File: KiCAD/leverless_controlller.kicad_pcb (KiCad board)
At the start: 2 copper layers, 251.4 x 138.3 mm, 31 parts, among them SW2 SW_Push, U1 RP2040, U2 NCP1117-3.3_SOT223, U3 W25Q16JVSS, Y1 ABM8-272-T3

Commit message: Start PCB Layout
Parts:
- added J1: USB_C_Receptacle_USB2.0_14P, Fightstick_Library:USB_C_Receptacle_HCTL_Fightstick_16P_TopMnt_Horizontal, F.Cu at (76.4, 30.7)
- added SW10_SHARE1: SW_Push, Fightstick_Library:Kailh_MX_Style_Keyswitch, F.Cu at (257.2, 46.9)
- added SW11_START1: SW_Push, Fightstick_Library:Kailh_MX_Style_Keyswitch, F.Cu at (257.2, 63.1)
- added SW12_THROW1: SW_Push, Fightstick_Library:Kailh_MX_Style_Keyswitch, F.Cu at (149.9, 60.3)
- added SW13_R3: SW_Push, Fightstick_Library:Kailh_MX_Style_Keyswitch, F.Cu at (257.2, 95.4)
- added SW14_PS1: SW_Push, Fightstick_Library:Kailh_MX_Style_Keyswitch, F.Cu at (257.2, 111.5)
- added SW15_TOUCHPAD1: SW_Push, Fightstick_Library:Kailh_MX_Style_Keyswitch, F.Cu at (257.2, 127.7)
- added SW16_UP1: SW_Push, Fightstick_Library:Kailh_MX_Style_Keyswitch, F.Cu at (150.4, 136.0)
- added SW17_UP2: SW_Push, Fightstick_Library:Kailh_MX_Style_Keyswitch, F.Cu at (117.1, 54.4)
- added SW18_DOWN1: SW_Push, Fightstick_Library:Kailh_MX_Style_Keyswitch, F.Cu at (109.8, 72.0)
- added SW19_LEFT1: SW_Push, Fightstick_Library:Kailh_MX_Style_Keyswitch, F.Cu at (92.2, 64.7)
- added SW20_RIGHT1: SW_Push, Fightstick_Library:Kailh_MX_Style_Keyswitch, F.Cu at (125.9, 83.0)
- added SW3_MK1: SW_Push, Fightstick_Library:Kailh_MX_Style_Keyswitch, F.Cu at (199.9, 90.0)
- added SW4_LP1: SW_Push, Fightstick_Library:Kailh_MX_Style_Keyswitch, F.Cu at (174.9, 75.0)
- added SW5_MP1: SW_Push, Fightstick_Library:Kailh_MX_Style_Keyswitch, F.Cu at (199.9, 61.0)
- added SW6_DI1: SW_Push, Fightstick_Library:Kailh_MX_Style_Keyswitch, F.Cu at (175.1, 46.0)
- added SW7_HP1: SW_Push, Fightstick_Library:Kailh_MX_Style_Keyswitch, F.Cu at (228.9, 61.0)
- added SW8_DP1: SW_Push, Fightstick_Library:Kailh_MX_Style_Keyswitch, F.Cu at (60.0, 72.0)
- added SW9_HK1: SW_Push, Fightstick_Library:Kailh_MX_Style_Keyswitch, F.Cu at (228.9, 90.0)
- S1: footprint keyswitches.pretty-2.1:Stabilizer_MX_2u -> Fightstick_Library:Kailh_MX_Style_Keyswitch
- SW2_LK1: renamed from SW2; footprint keyswitches.pretty-2.1:Kailh_socket_MX -> Fightstick_Library:Kailh_MX_Style_Keyswitch
- moved C2 100.1 mm to (59.9, 40.6), turned to 180 degrees
- moved C1 94.0 mm to (68.9, 35.7), turned to 180 degrees
- moved R1 92.3 mm to (69.5, 33.7), turned to 180 degrees
- moved U2 90.5 mm to (65.9, 40.7), turned to 180 degrees
- moved C5 89.7 mm to (72.9, 45.5), turned to 180 degrees
- moved R2 87.8 mm to (73.9, 37.2), turned to -90 degrees
- moved R6 87.6 mm to (70.6, 50.4), turned to -90 degrees
- moved R5 87.1 mm to (68.3, 53.1)
- moved R3 86.1 mm to (78.4, 36.3)
- moved SW2_LK1 75.7 mm to (174.9, 104.0)
- moved C4 74.8 mm to (95.9, 39.4), turned to 180 degrees
- moved R4 73.4 mm to (91.4, 42.9), turned to 180 degrees
- moved C17 68.6 mm to (83.6, 36.3), turned to 90 degrees
- moved C3 68.5 mm to (99.0, 43.2), turned to -90 degrees
- moved C16 67.2 mm to (82.5, 36.3), turned to 90 degrees
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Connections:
- SW2_LK1 pad 1: A1 -> B1
- U1 pad 34: unconnected-(U1-GPIO22-Pad34) -> UP2
- U1 pad 4: UP -> UP1
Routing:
- net +3.3V: track 0.00 -> 66.5 mm
- net /Main/QSPI_SS: track 0.00 -> 28.9 mm
- net +1V1: track 0.00 -> 18.2 mm
- net /Main/QSPI_SD1: track 0.00 -> 15.2 mm
- net /Main/XIN: track 0.00 -> 12.4 mm
- net /Main/QSPI_SD2: track 0.00 -> 11.9 mm
- net VBUS: track 0.00 -> 10.8 mm
- net /Main/D+: track 0.00 -> 10.6 mm
- net /Main/D-: track 0.00 -> 8.32 mm
- net /Main/QSPI_SD3: track 0.00 -> 6.70 mm
- net /Main/QSPI_SCLK: track 0.00 -> 6.15 mm
- net Net-(C4-Pad2): track 0.00 -> 6.10 mm
- net /Main/QSPI_SD0: track 0.00 -> 4.63 mm
- net /Main/XOUT: track 0.00 -> 3.02 mm
- net Net-(U1-USB_DP): track 0.00 -> 2.55 mm
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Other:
- board outline removed

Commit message: PCB First Draft
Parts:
- removed C17: 100n, Capacitor_SMD:C_0402_1005Metric
- removed SW13_R3: SW_Push, Fightstick_Library:Kailh_MX_Style_Keyswitch
- added ?: , , F.Cu at (83.8, 41.9)
- added ?: , , F.Cu at (85.9, 41.9)
- added ?: , , F.Cu at (85.9, 40.9)
- added ?: , , F.Cu at (85.9, 42.9)
- added ?: , , F.Cu at (84.8, 42.9)
- added ?: , , F.Cu at (84.8, 40.9)
- added ?: , , F.Cu at (84.8, 41.9)
- added ?: , , F.Cu at (83.8, 42.9)
- added ?: , , F.Cu at (83.8, 40.9)
- added J2: Conn_01x03_Socket, Fightstick_Library:Debug_Points, F.Cu at (97.8, 36.5)
- added SW1: SW_DIP_x01, Fightstick_Library:SW_SMD_BUTTON_YTS_A007, F.Cu at (55.2, 37.2)
- added SW2_MODE1: SW_SPST, Button_Switch_THT:SW_SPST_Omron_B3F-40xx, F.Cu at (58.0, 51.0)
- S1: footprint Fightstick_Library:Kailh_MX_Style_Keyswitch -> PCM_Mounting_Keyboard_Stabilizer:Stabilizer_Cherry_MX_2.00u
- SW10_SHARE1, SW11_START1, SW14_PS1, SW15_TOUCHPAD1: footprint Fightstick_Library:Kailh_MX_Style_Keyswitch -> Button_Switch_THT:SW_SPST_Omron_B3F-40xx
- moved SW15_TOUCHPAD1 82.7 mm to (242.5, 46.2), turned to 90 degrees
- moved SW14_PS1 71.7 mm to (227.5, 46.2), turned to 90 degrees
- moved SW11_START1 62.0 mm to (197.5, 46.2), turned to 90 degrees
- moved SW10_SHARE1 44.7 mm to (212.5, 46.2), turned to 90 degrees
- moved S1 37.2 mm to (150.4, 136.0)
- moved C5 6.90 mm to (72.1, 52.3), turned to 0 degrees
- moved R5 6.75 mm to (63.9, 48.0)
- moved C2 5.43 mm to (62.9, 36.1), turned to 90 degrees
- moved R6 3.08 mm to (67.7, 49.4)
- moved U3 2.62 mm to (74.9, 48.5), turned to 180 degrees
- moved R4 1.14 mm to (92.6, 42.9)
- moved C16 1.00 mm to (83.5, 36.0)
- moved C3 0.90 mm to (99.0, 42.3)
- moved Y1 0.90 mm to (96.3, 41.6)
- moved C4 0.90 mm to (95.9, 38.5)
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- renumbered SW16_UP1 to SW16_SPACE1, SW17_UP2 to SW17_W1
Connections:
- net UP1 renamed SPACE
- SW17_W1 pad 1: UP2 -> W
- U1 pad 11: R2 -> B2
- U1 pad 12: L2 -> R2
- U1 pad 14: B4 -> L3
- U1 pad 15: R1 -> B4
- U1 pad 16: L1 -> R1
- U1 pad 17: TURBO -> A2
- U1 pad 18: T LED -> unconnected-(U1-GPIO15-Pad18)
- U1 pad 2: SDA -> MODE
- U1 pad 26: /Main/RUN -> +3.3V
- U1 pad 27: S1 -> A1
- U1 pad 28: S2 -> L1
- U1 pad 29: L3 -> S1
- U1 pad 3: SLC -> L2
- U1 pad 30: R3 -> S2
- U1 pad 31: A1 -> unconnected-(U1-GPIO20-Pad31)
- U1 pad 32: A2 -> unconnected-(U1-GPIO21-Pad32)
- U1 pad 34: UP2 -> unconnected-(U1-GPIO22-Pad34)
- U1 pad 5: DOWN -> LEFT
- U1 pad 6: RIGHT -> DOWN
- U1 pad 7: LEFT -> RIGHT
- U1 pad 8: B1 -> W
- U1 pad 9: B2 -> B1
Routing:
- net GND: track 0.00 -> 654.5 mm, vias 0 -> 11
- net A2: track 0.00 -> 171.3 mm
- net R2: track 0.00 -> 166.8 mm, vias 0 -> 1
- net A1: track 0.00 -> 160.8 mm
- net R1: track 0.00 -> 153.1 mm, vias 0 -> 1
- net S1: track 0.00 -> 141.1 mm
- net B2: track 0.00 -> 138.7 mm, vias 0 -> 1
- net B4: track 0.00 -> 134.2 mm, vias 0 -> 1
- net S2: track 0.00 -> 127.0 mm
- net B1: track 0.00 -> 124.7 mm, vias 0 -> 1
- net SPACE: track 0.00 -> 124.7 mm, vias 0 -> 1
- net B3: track 0.00 -> 106.0 mm, vias 0 -> 1
- net L1: track 0.00 -> 99.0 mm, vias 0 -> 1
- net +3.3V: track 66.5 -> 144.8 mm, vias 0 -> 5
- net L3: track 0.00 -> 74.4 mm, vias 0 -> 1
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- added copper zone on B.Cu, net GND
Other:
- board outline added: 213 x 123 mm

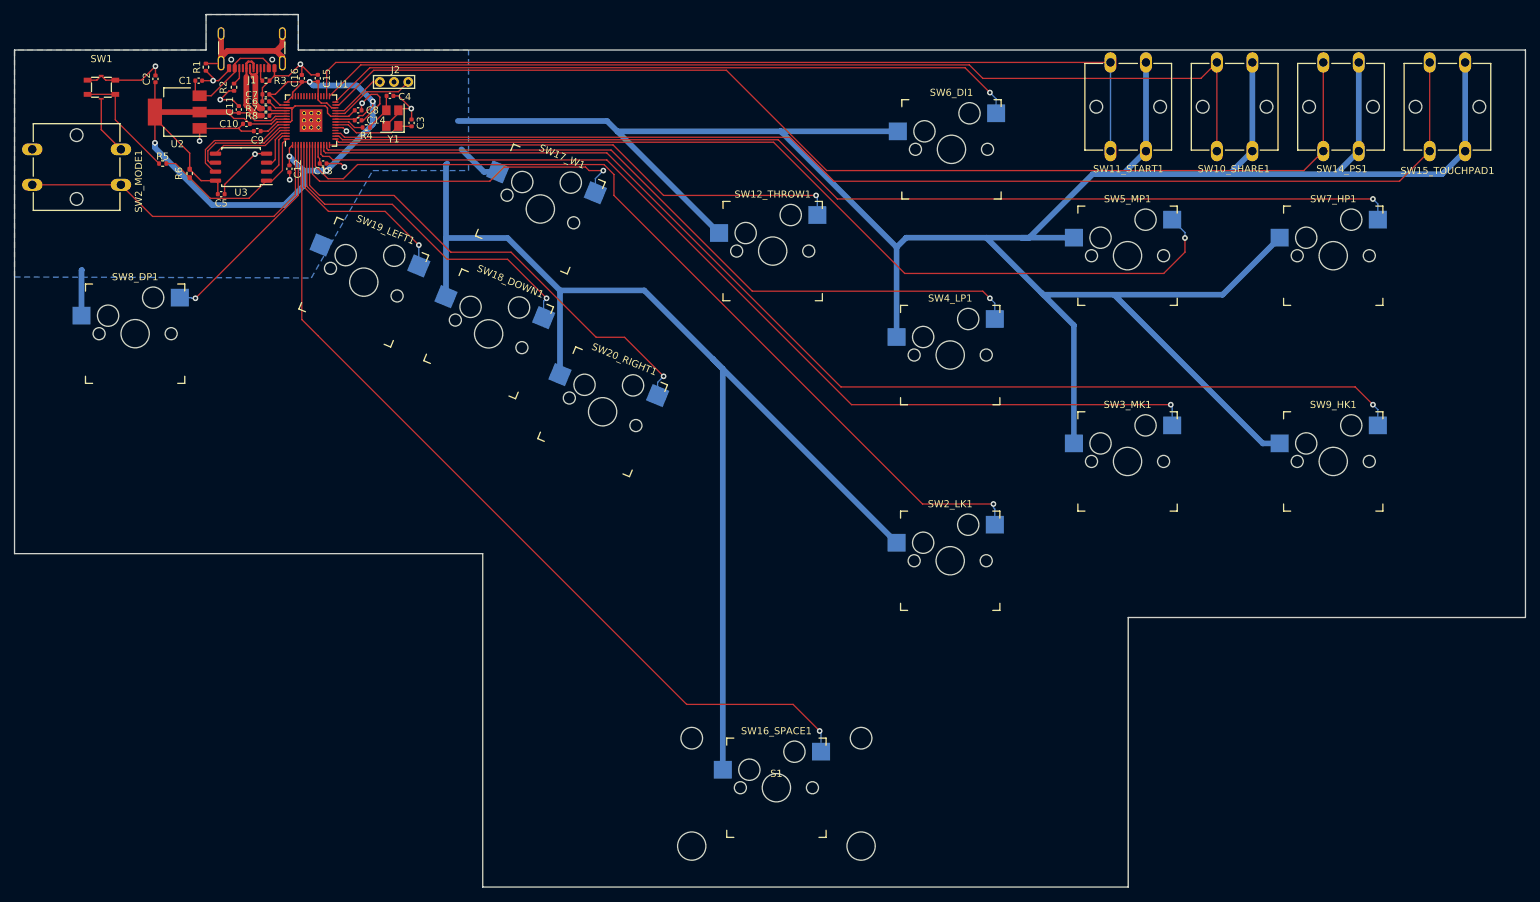
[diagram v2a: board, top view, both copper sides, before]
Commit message: Make PCB and case fit together
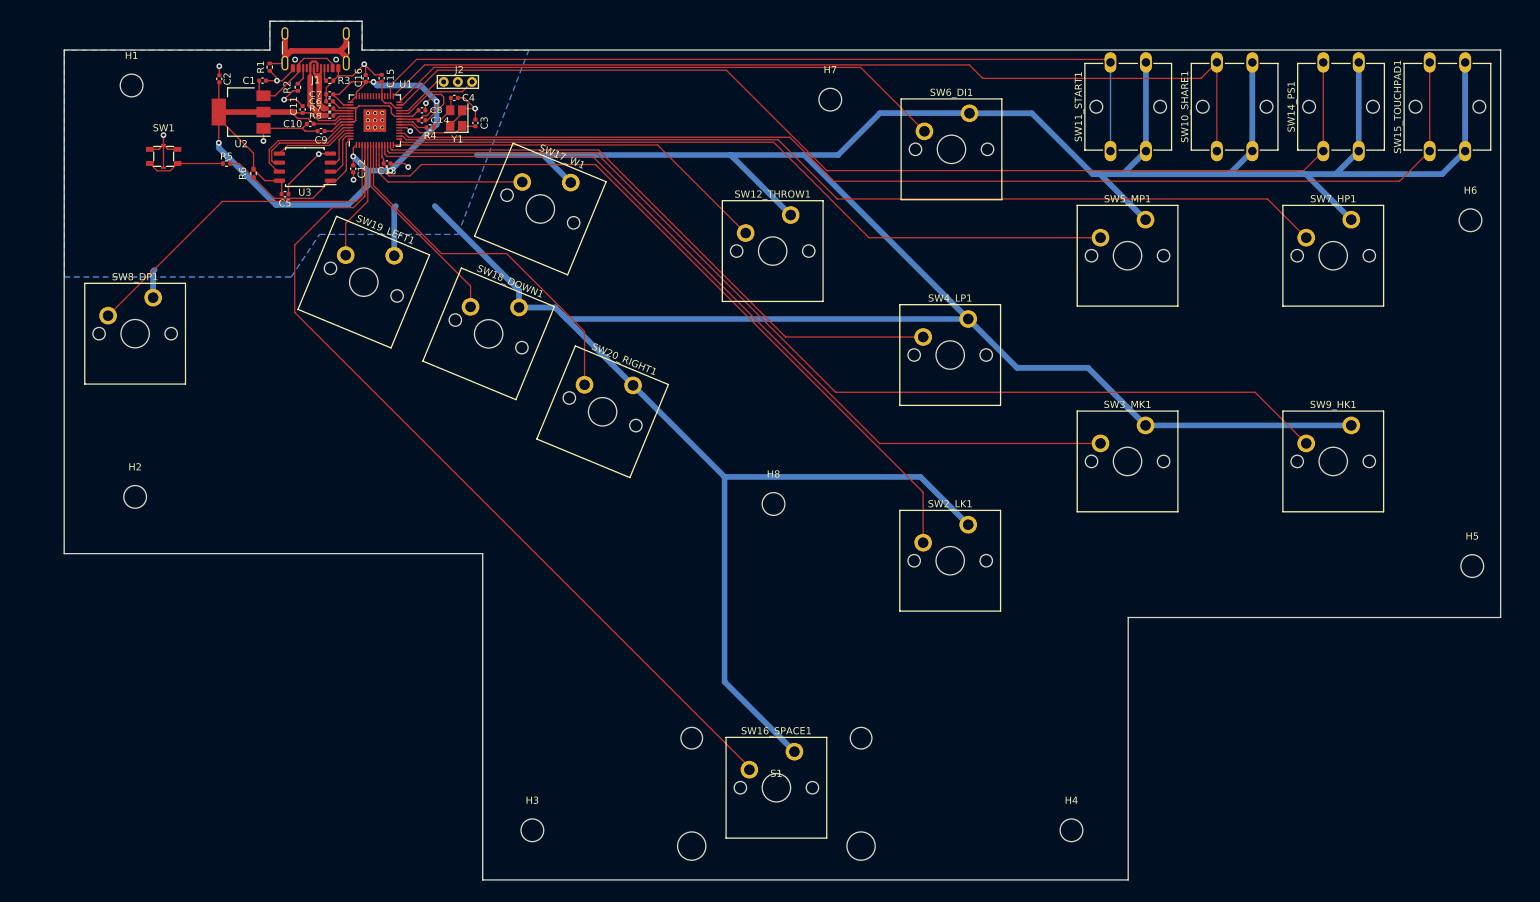
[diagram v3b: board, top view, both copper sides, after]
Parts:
- removed SW2_MODE1: SW_SPST, Button_Switch_THT:SW_SPST_Omron_B3F-40xx
- added H1: MountingHole, MountingHole:MountingHole_3.2mm_M3, F.Cu at (59.5, 37.0)
- added H2: MountingHole, MountingHole:MountingHole_3.2mm_M3, F.Cu at (60.0, 95.0)
- added H3: MountingHole, MountingHole:MountingHole_3.2mm_M3, F.Cu at (116.0, 142.0)
- added H4: MountingHole, MountingHole:MountingHole_3.2mm_M3, F.Cu at (192.0, 142.0)
- added H5: MountingHole, MountingHole:MountingHole_3.2mm_M3, F.Cu at (248.5, 104.8)
- added H6: MountingHole, MountingHole:MountingHole_3.2mm_M3, F.Cu at (248.2, 56.0)
- added H7: MountingHole, MountingHole:MountingHole_3.2mm_M3, F.Cu at (158.0, 39.0)
- added H8: MountingHole, MountingHole:MountingHole_3.2mm_M3, F.Cu at (150.0, 96.0)
- SW12_THROW1, SW16_SPACE1, SW2_LK1, SW3_MK1, SW4_LP1, SW5_MP1, SW6_DI1, SW7_HP1, SW8_DP1, SW9_HK1: footprint Fightstick_Library:Kailh_MX_Style_Keyswitch -> PCM_Switch_Keyboard_Cherry_MX:SW_Cherry_MX_PCB
- SW17_W1, SW18_DOWN1, SW19_LEFT1, SW20_RIGHT1: footprint Fightstick_Library:Kailh_MX_Style_Keyswitch -> PCM_Switch_Keyboard_Cherry_MX:SW_Cherry_MX_PCB_1.00u
- moved SW1 13.1 mm to (64.0, 47.0)
- moved C4 9.08 mm to (105.0, 38.8)
- moved ? 9.00 mm to (92.8, 41.9)
- moved ? 9.00 mm to (94.9, 41.9)
- moved ? 9.00 mm to (94.9, 40.9)
- moved ? 9.00 mm to (94.9, 42.9)
- moved ? 9.00 mm to (93.8, 42.9)
- moved ? 9.00 mm to (93.8, 40.9)
- moved ? 9.00 mm to (93.8, 41.9)
- moved ? 9.00 mm to (92.8, 42.9)
- moved ? 9.00 mm to (92.8, 40.9)
- moved C1 9.00 mm to (78.0, 36.3)
- moved C10 9.00 mm to (84.7, 42.4)
- moved C11 9.00 mm to (83.6, 40.4)
- moved C12 9.00 mm to (90.8, 48.8)
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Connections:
- U1 pad 2: MODE -> unconnected-(U1-GPIO0-Pad2)
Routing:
- net MODE: track 47.2 -> 0.00 mm
- net B4: track 134.2 -> 104.6 mm, vias 1 -> 0
- net GND: track 654.5 -> 628.0 mm, vias 11 -> 12
- net W: track 50.2 -> 24.8 mm, vias 1 -> 0
- net DOWN: track 49.1 -> 28.7 mm, vias 1 -> 0
- net L2: track 29.9 -> 49.9 mm, vias 1 -> 0
- net B2: track 138.7 -> 119.1 mm, vias 1 -> 0
- net L3: track 74.4 -> 54.8 mm, vias 1 -> 0
- net R2: track 166.8 -> 147.4 mm, vias 1 -> 0
- net R1: track 153.1 -> 133.8 mm, vias 1 -> 0
- net B3: track 106.0 -> 86.6 mm, vias 1 -> 0
- net L1: track 99.0 -> 79.8 mm, vias 1 -> 0
- net RIGHT: track 69.8 -> 51.5 mm, vias 1 -> 0
- net B1: track 124.7 -> 107.2 mm, vias 1 -> 0
- net LEFT: track 28.5 -> 16.8 mm, vias 1 -> 0
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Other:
- board size 213 x 123 mm -> 202.5 x 121.1 mm

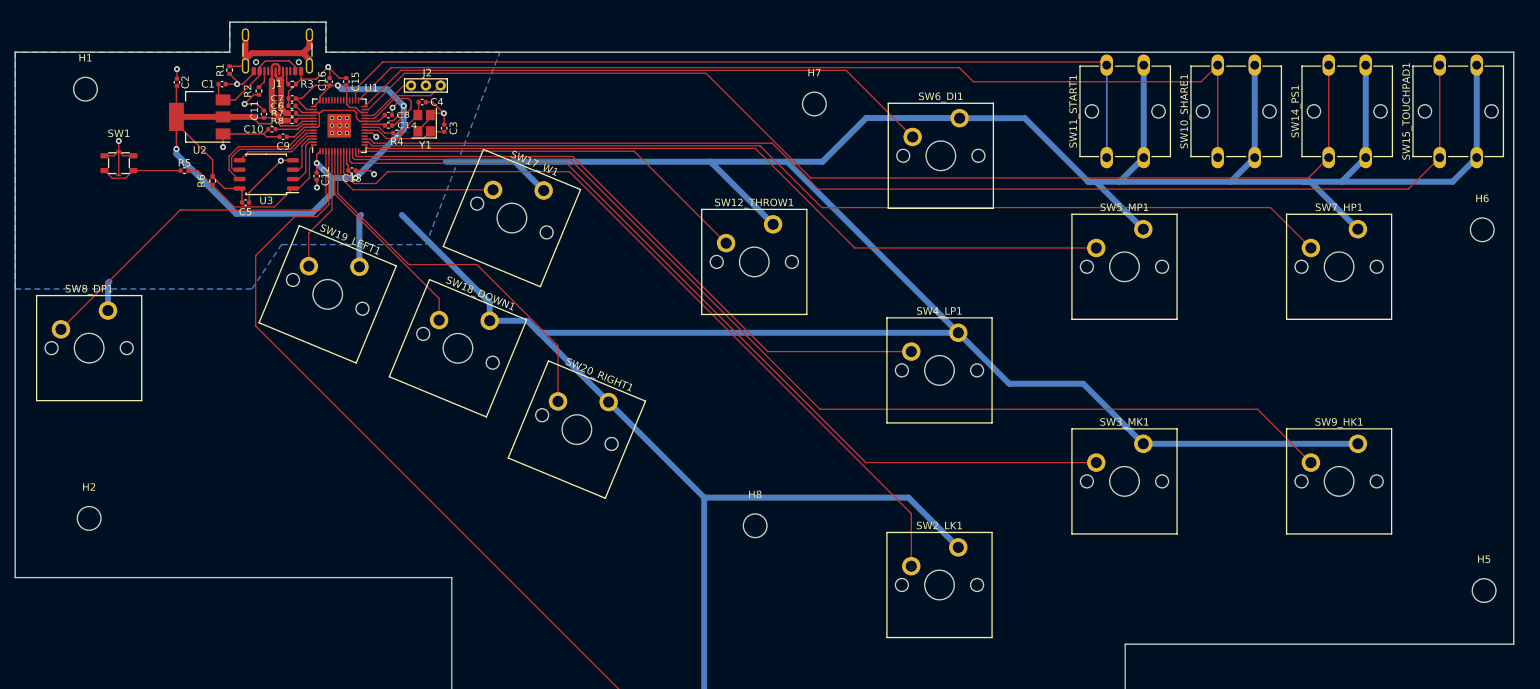
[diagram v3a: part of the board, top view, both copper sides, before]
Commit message: First DFM pass
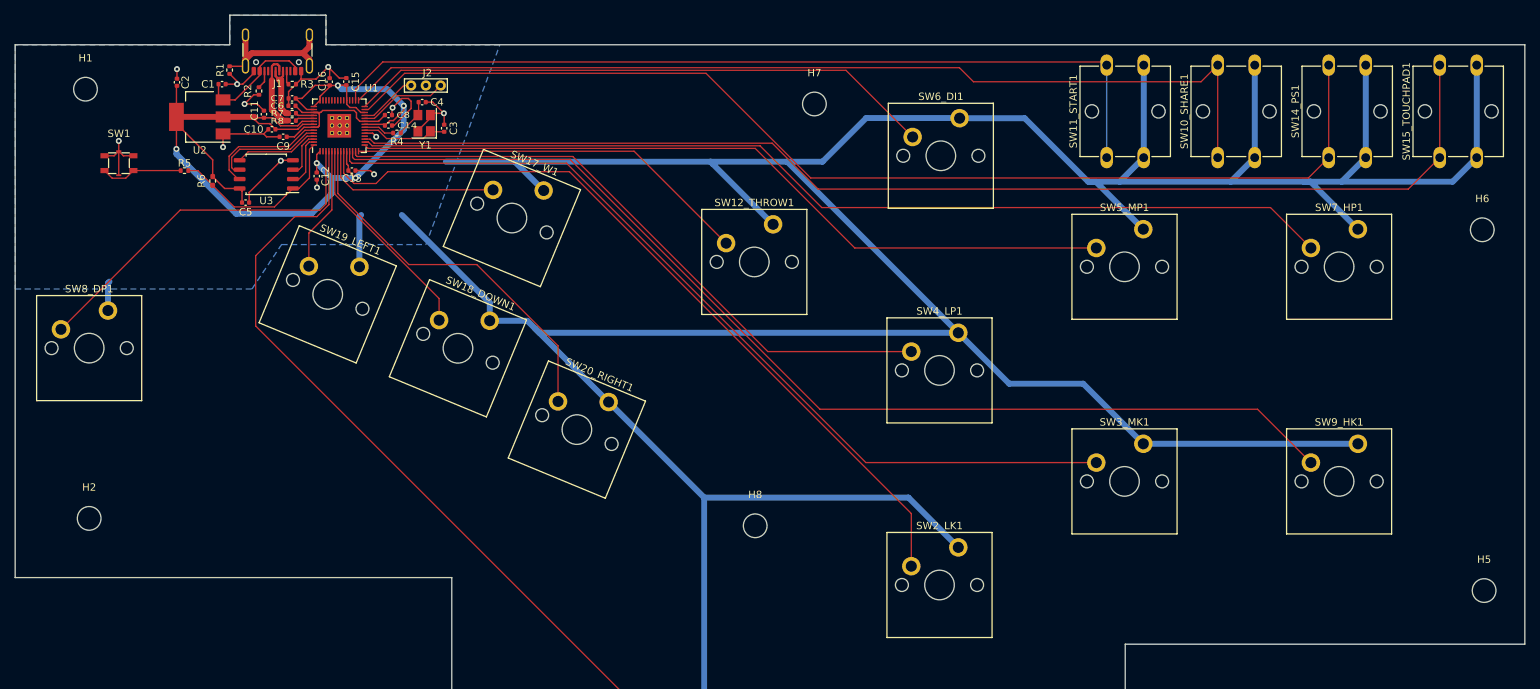
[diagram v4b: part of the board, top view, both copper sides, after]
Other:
- board size 202.5 x 121.1 mm -> 204 x 122 mm

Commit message: Second DFM pass
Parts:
- moved J1 2.09 mm to (85.5, 28.7)
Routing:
- net GND: track 628.0 -> 631.8 mm
- net /Main/D+: track 10.6 -> 12.9 mm
- net VBUS: track 16.4 -> 18.5 mm
- net Net-(J1-CC2): track 2.49 -> 4.60 mm
- net Net-(J1-CC1): track 1.87 -> 3.93 mm
- net /Main/D-: track 8.32 -> 10.1 mm
- net Net-(J1-SHIELD): track 20.4 -> 19.4 mm
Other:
- board size 204 x 122 mm -> 204 x 124 mm
